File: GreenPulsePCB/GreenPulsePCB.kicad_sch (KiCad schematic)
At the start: 6 parts, among them J1 Conn_01x02_Pin, U1 BME280

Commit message: LEDs added
LEDs added (inc. data sheets and hyperlinks) as well as schematics view (screenshot)
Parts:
- added D1: LED_Gruen, symbol Device:LED
- added D2: LED_Gelb, symbol Device:LED
- added D3: LED_Rot, symbol Device:LED
- added D4: LED_Blau, symbol Device:LED
- added R3: 82, symbol Device:R
- added R4: 0, symbol Device:R
- added R5: 91, symbol Device:R
- added R6: R, symbol Device:R
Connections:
- net GND: now also D1.1 (K), D2.1 (K), D3.1 (K), D4.1 (K)
- net 3.3 renamed V_DDIO 3.3
- net V_DDIO 3.3: no longer C1.1, U1.8 (VDD)
- new net: D1.2 (A), R3.2
- new net: D4.2 (A), R6.2
- new net: D2.2 (A), R4.2
- new net: D3.2 (A), R5.2
- new net VCC 3.3: R3.1, R4.1, R5.1, R6.1
- new net V_DD 3.3: C1.1, U1.8 (VDD)
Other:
- moved on the sheet: C1, C2, J1, R1, R2, U1

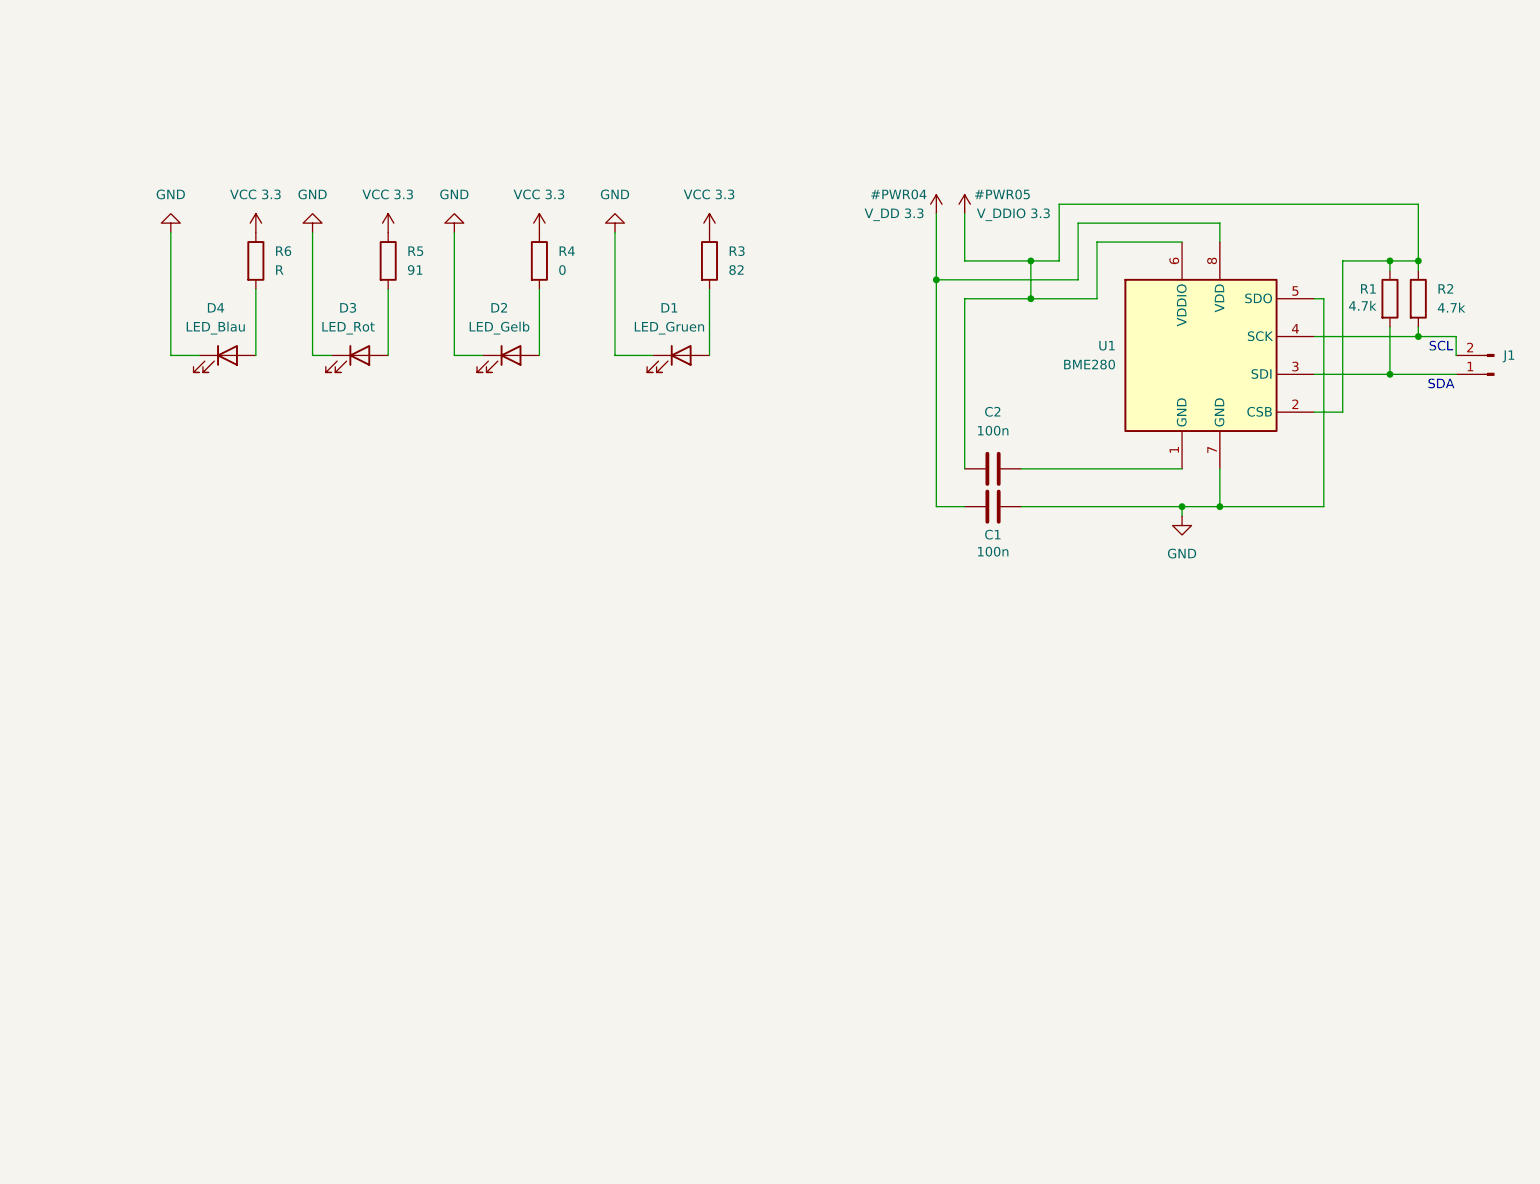
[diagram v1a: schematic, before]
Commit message: Schaltplan fertiggestellt
Transistoren hinzugefügt um Schaltung der LEDs zu ermöglichen. Vorwiderstände der LEDs müssen noch berechnet werden. Auch Schaltung des BME280 nochmal überprüfen.
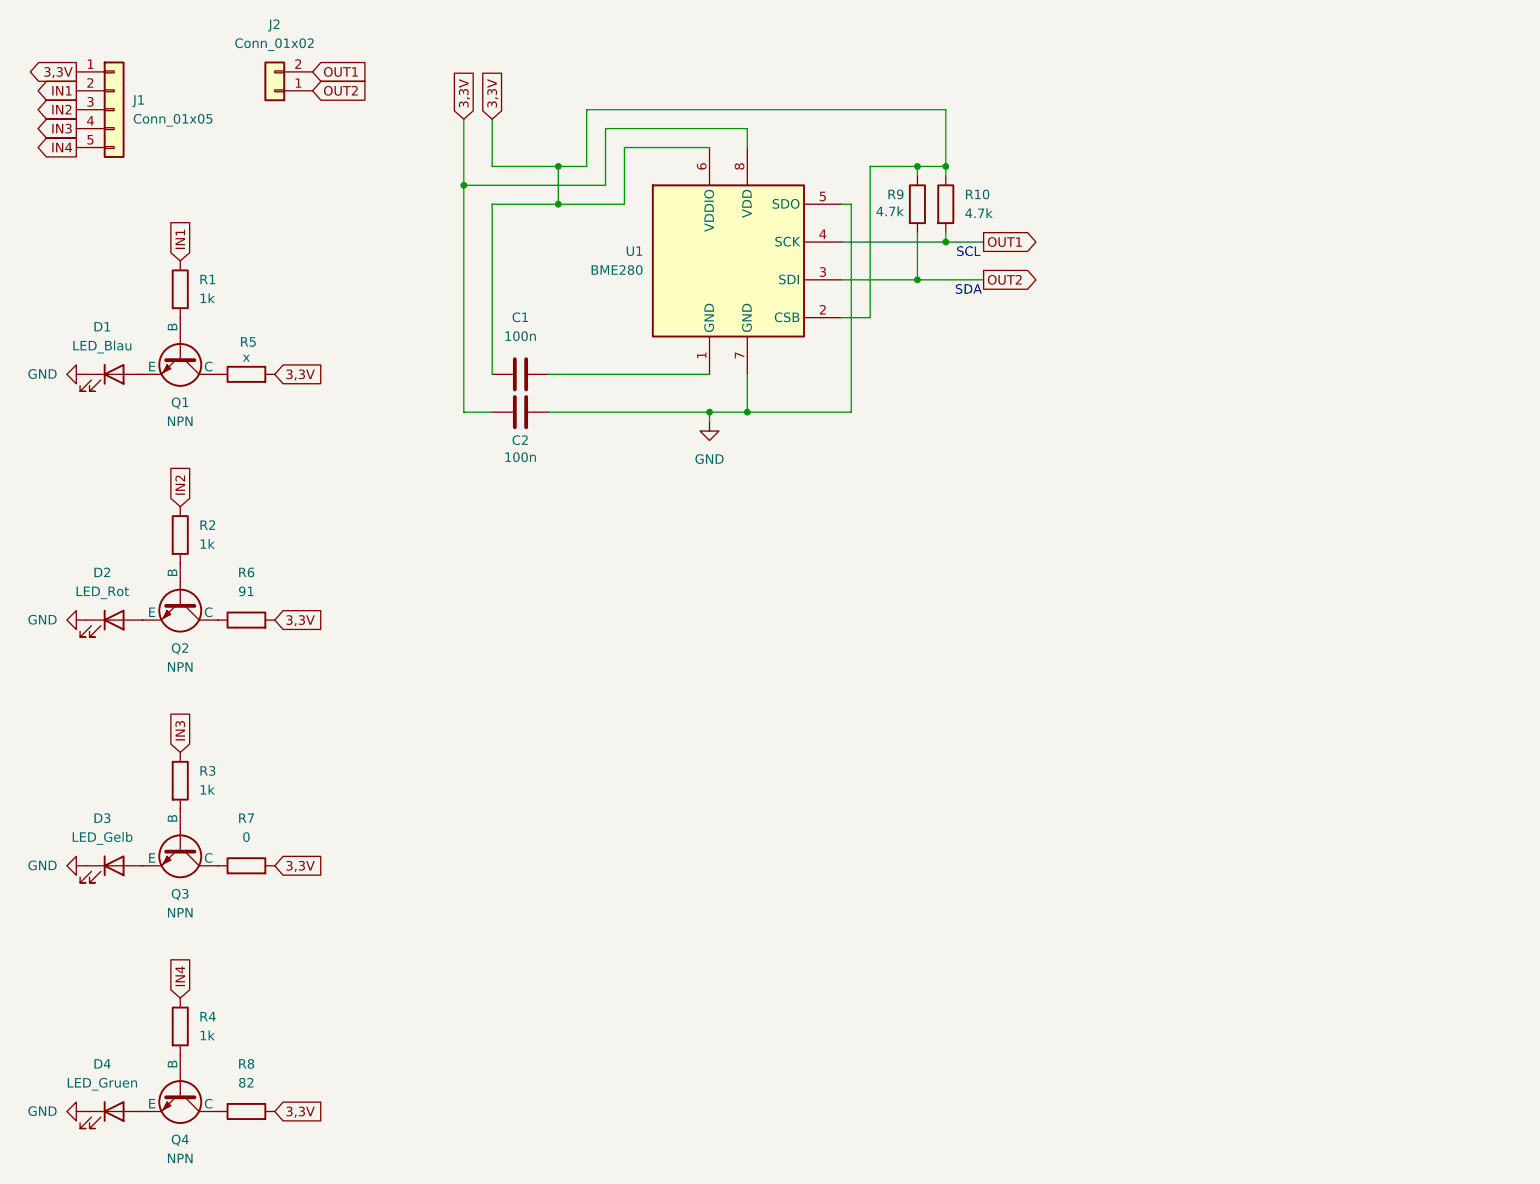
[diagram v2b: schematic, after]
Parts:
- removed J1: Conn_01x02_Pin, symbol Connector:Conn_01x02_Pin
- added J1: Conn_01x05, symbol Connector_Generic:Conn_01x05
- added J2: Conn_01x02, symbol Connector_Generic:Conn_01x02
- added Q1, Q2, Q3, Q4: NPN, symbol Simulation_SPICE:NPN
- added R1, R2, R3, R4: 1k, symbol Device:R
- R5: renamed from R6; value R -> x
- renumbered C2 to C1, C1 to C2, D4 to D1, D3 to D2, D2 to D3, D1 to D4, R2 to R10, R5 to R6, R4 to R7, R3 to R8, R1 to R9
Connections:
- net V_DDIO 3.3 is gone; now on net 3,3V: C1.2, R10.1, R9.1, U1.2 (CSB), U1.6 (VDDIO)
- net OUT2: now reaches R9.2, U1.3 (SDI)
- net OUT2: now also J2.1 (Pin_1)
- net OUT1: now reaches R10.2, U1.4 (SCK)
- net OUT1: now also J2.2 (Pin_2)
- net at D4.2 (A): now also Q4.3 (E); no longer R8.2
- net at D1.2 (A): now also Q1.3 (E); no longer R5.2
- net at D3.2 (A): now also Q3.3 (E); no longer R7.2
- net at D2.2 (A): now also Q2.3 (E); no longer R6.2
- removed net VCC 3.3: R5.1, R6.1, R7.1, R8.1
- net V_DD 3.3 renamed 3,3V
- net 3,3V: now also R5.2, R6.2, R7.2, R8.2, J1.1 (Pin_1)
- new net: Q4.1 (C), R8.1
- new net: Q4.2 (B), R4.2
- new net: Q1.1 (C), R5.1
- new net: Q2.1 (C), R6.1
- new net: Q3.1 (C), R7.1
- new net: Q3.2 (B), R3.2
- new net: Q1.2 (B), R1.2
- new net: Q2.2 (B), R2.2
- new net IN1: J1.2 (Pin_2), R1.1
- new net IN2: J1.3 (Pin_3), R2.1
- new net IN3: J1.4 (Pin_4), R3.1
- new net IN4: J1.5 (Pin_5), R4.1
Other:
- moved on the sheet: C1, C2, D1, D2, D3, D4, R10, R5, R6, R7, R8, R9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

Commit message: Footprints zugewiesen
Allen Bauteilen ihre Footprints zugewiesen.
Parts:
- C1, C2: footprint (none) -> Capacitor_SMD:C_0805_2012Metric
- D1, D2, D3, D4: footprint (none) -> LED_SMD:LED_0805_2012Metric
- J1: footprint (none) -> Connector_PinSocket_2.54mm:PinSocket_1x05_P2.54mm_Horizontal
- J2: footprint (none) -> Connector_PinSocket_2.54mm:PinSocket_1x02_P2.54mm_Horizontal
- Q1, Q2, Q3, Q4: footprint (none) -> Package_TO_SOT_SMD:SOT-23
- R1, R10, R2, R3, R4, R5, R6, R7, R8, R9: footprint (none) -> Resistor_SMD:R_0805_2012Metric
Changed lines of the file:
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@@
 			)
 		)
-		(property "Footprint" ""
+		(property "Footprint" "Package_TO_SOT_SMD:SOT-23"
 			(at 38.1 222.25 0)
 			(effects
@@
 			)
 		)
-		(property "Footprint" ""
+		(property "Footprint" "LED_SMD:LED_0805_2012Metric"
 			(at 29.21 161.29 0)
 			(effects
@@
 			)
 		)
-		(property "Footprint" ""
+		(property "Footprint" "Resistor_SMD:R_0805_2012Metric"
 			(at 46.99 64.008 90)
 			(effects
@@
 			)
 		)
-		(property "Footprint" ""
+		(property "Footprint" "LED_SMD:LED_0805_2012Metric"
 			(at 29.21 62.23 0)
 			(effects
@@
 			)
 		)
-		(property "Footprint" ""
+		(property "Footprint" "Capacitor_SMD:C_0805_2012Metric"
 			(at 80.01 63.1952 0)
 			(effects
@@
 			)
 		)
-		(property "Footprint" ""
+		(property "Footprint" "LED_SMD:LED_0805_2012Metric"
 			(at 29.21 128.27 0)
 			(effects
@@
 			)
 		)
-		(property "Footprint" ""
+		(property "Footprint" "Resistor_SMD:R_0805_2012Metric"
 			(at 46.99 97.028 90)
 			(effects
@@
 			)
 		)
-		(property "Footprint" ""
+		(property "Footprint" "Resistor_SMD:R_0805_2012Metric"
 			(at 46.99 130.048 90)
 			(effects
@@
 			)
 		)
-		(property "Footprint" ""
+		(property "Footprint" "Resistor_SMD:R_0805_2012Metric"
 			(at 36.322 149.86 90)
 			(effects
@@
 			)
 		)
-		(property "Footprint" ""
+		(property "Footprint" "Package_TO_SOT_SMD:SOT-23"
 			(at 38.1 189.23 0)
 			(effects
@@
 			)
 		)
-		(property "Footprint" ""
+		(property "Footprint" "Resistor_SMD:R_0805_2012Metric"
 			(at 36.322 116.84 90)
 			(effects
@@
 			)
 		)
-		(property "Footprint" ""
+		(property "Footprint" "Resistor_SMD:R_0805_2012Metric"
 			(at 135.382 39.37 90)
 			(effects
@@
 			)
 		)
-		(property "Footprint" ""
+		(property "Footprint" "Connector_PinSocket_2.54mm:PinSocket_1x02_P2.54mm_Horizontal"
 			(at 50.8 24.13 0)
 			(effects
@@
 			)
 		)
-		(property "Footprint" ""
+		(property "Footprint" "Capacitor_SMD:C_0805_2012Metric"
 			(at 87.63 66.3448 0)
 			(effects
@@
 			)
 		)
-		(property "Footprint" ""
+		(property "Footprint" "Resistor_SMD:R_0805_2012Metric"
 			(at 36.322 50.8 90)
 			(effects
@@
 			)
 		)
-		(property "Footprint" ""
+		(property "Footprint" "Connector_PinSocket_2.54mm:PinSocket_1x05_P2.54mm_Horizontal"
 			(at 29.21 26.67 0)
 			(effects
@@
 			)
 		)
-		(property "Footprint" ""
+		(property "Footprint" "Package_TO_SOT_SMD:SOT-23"
 			(at 38.1 156.21 0)
 			(effects
@@
 			)
 		)
-		(property "Footprint" ""
+		(property "Footprint" "Package_TO_SOT_SMD:SOT-23"
 			(at 38.1 123.19 0)
 			(effects
@@
 			)
 		)
-		(property "Footprint" ""
+		(property "Footprint" "Resistor_SMD:R_0805_2012Metric"
 			(at 36.322 83.82 90)
 			(effects
@@
 			)
 		)
-		(property "Footprint" ""
+		(property "Footprint" "Resistor_SMD:R_0805_2012Metric"
 			(at 46.99 163.068 90)
 			(effects
@@
 			)
 		)
-		(property "Footprint" ""
+		(property "Footprint" "LED_SMD:LED_0805_2012Metric"
 			(at 29.21 95.25 0)
 			(effects
@@
 			)
 		)
-		(property "Footprint" ""
+		(property "Footprint" "Resistor_SMD:R_0805_2012Metric"
 			(at 139.192 39.37 90)
 			(effects

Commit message: Platzierung vorläufig abgeschlossen
Noch auf Plausibilität / kürzeste Pfade prüfen. Routen der Pfade ist noch nicht erfolgt!
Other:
- title: (none) -> GreenPulsePCB
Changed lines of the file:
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@@
 	(generator_version "8.0")
 	(paper "A4")
+	(title_block
+		(title "GreenPulsePCB")
+		(date "2025-01-24")
+		(rev "0.1")
+	)
 	(junction
 		(at 140.97 34.29)

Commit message: Routing abgeschlossen
Kann trotzdem noch Fehler beinhalten. Nochmal gründlich überprüfen!
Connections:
- net OUT1: now also J2.1 (Pin_1); no longer J2.2 (Pin_2)
- net OUT2: now also J2.2 (Pin_2); no longer J2.1 (Pin_1)
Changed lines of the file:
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@@
 		)
 	)
-	(global_label "OUT1"
+	(global_label "OUT2"
 		(shape input)
 		(at 55.88 21.59 0)
@@
 		)
 	)
-	(global_label "OUT2"
+	(global_label "OUT1"
 		(shape input)
 		(at 55.88 24.13 0)
